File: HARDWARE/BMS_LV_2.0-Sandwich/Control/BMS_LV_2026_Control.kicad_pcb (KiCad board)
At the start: 4 copper layers, 62.5 x 36.4 mm, 59 parts, among them IC1 TAR5S33UTE85LF, IC2 M24M02E-UFMN6TP, IC4 TPS54202HDDCR, J1 Conn_01x26, U1 STM32G484RETx, U7 ADM3057ExRW, Y1 ATX-11-F-32.000MHZ-F05-T

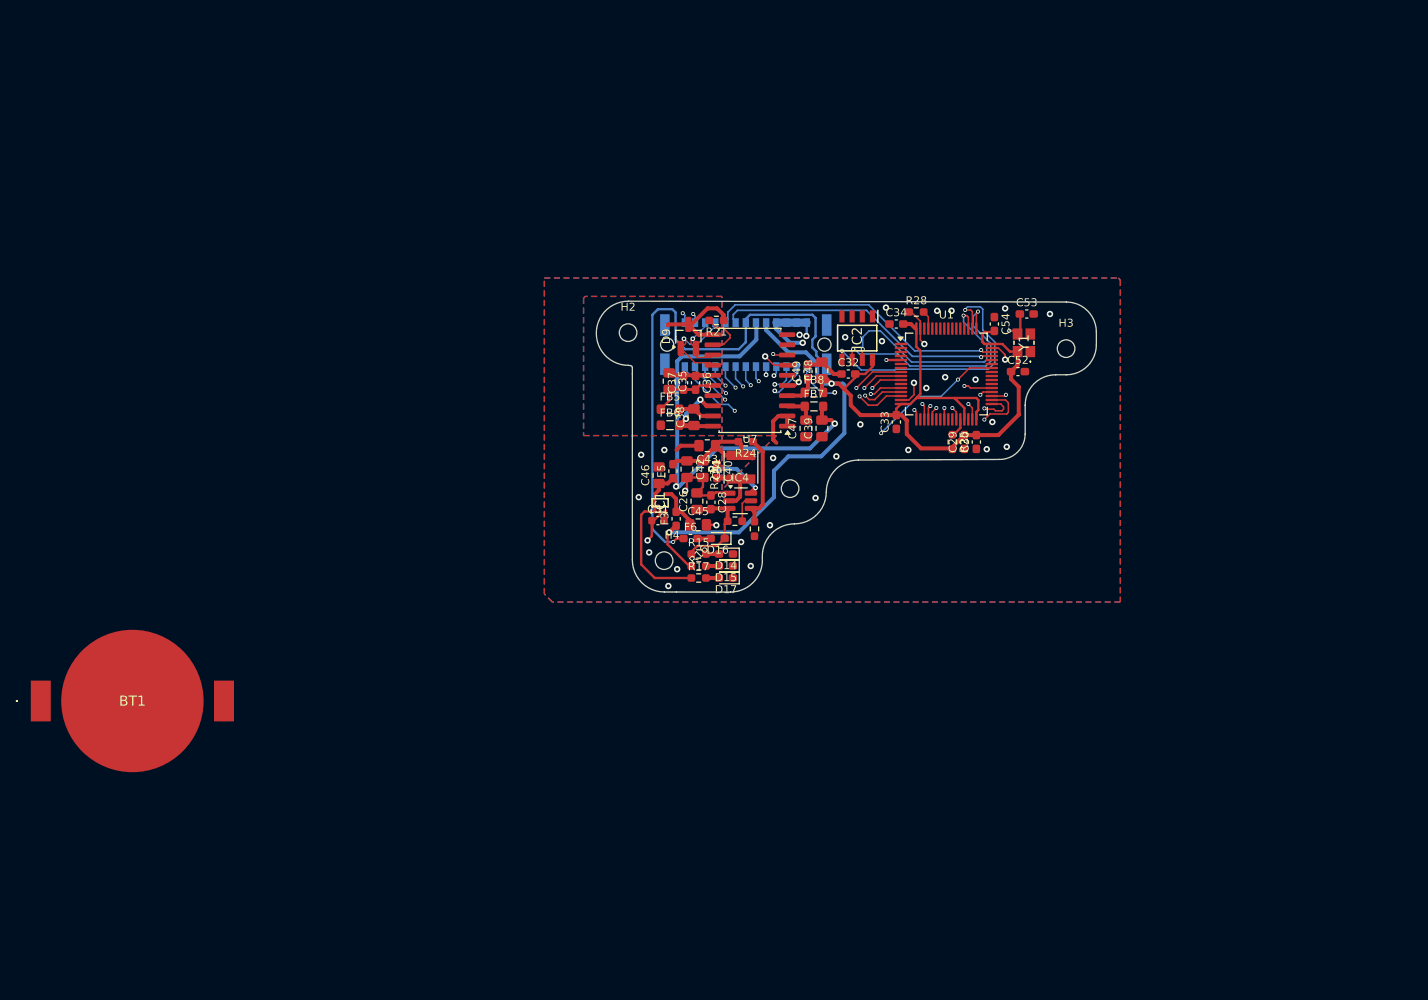
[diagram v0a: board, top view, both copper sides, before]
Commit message: Zmiany w power: nowe bezpieczniki, nowy wymienialny layout dla tych bezpiecznikow, dodano diode zenera dla stabilizacji napięcia, zmiany dla control:  wyjebany eeprom, przesunięty can, zmieniony layout przetwornic, dodano programator i tvs, jeszcze do dokonczenia routing w control.
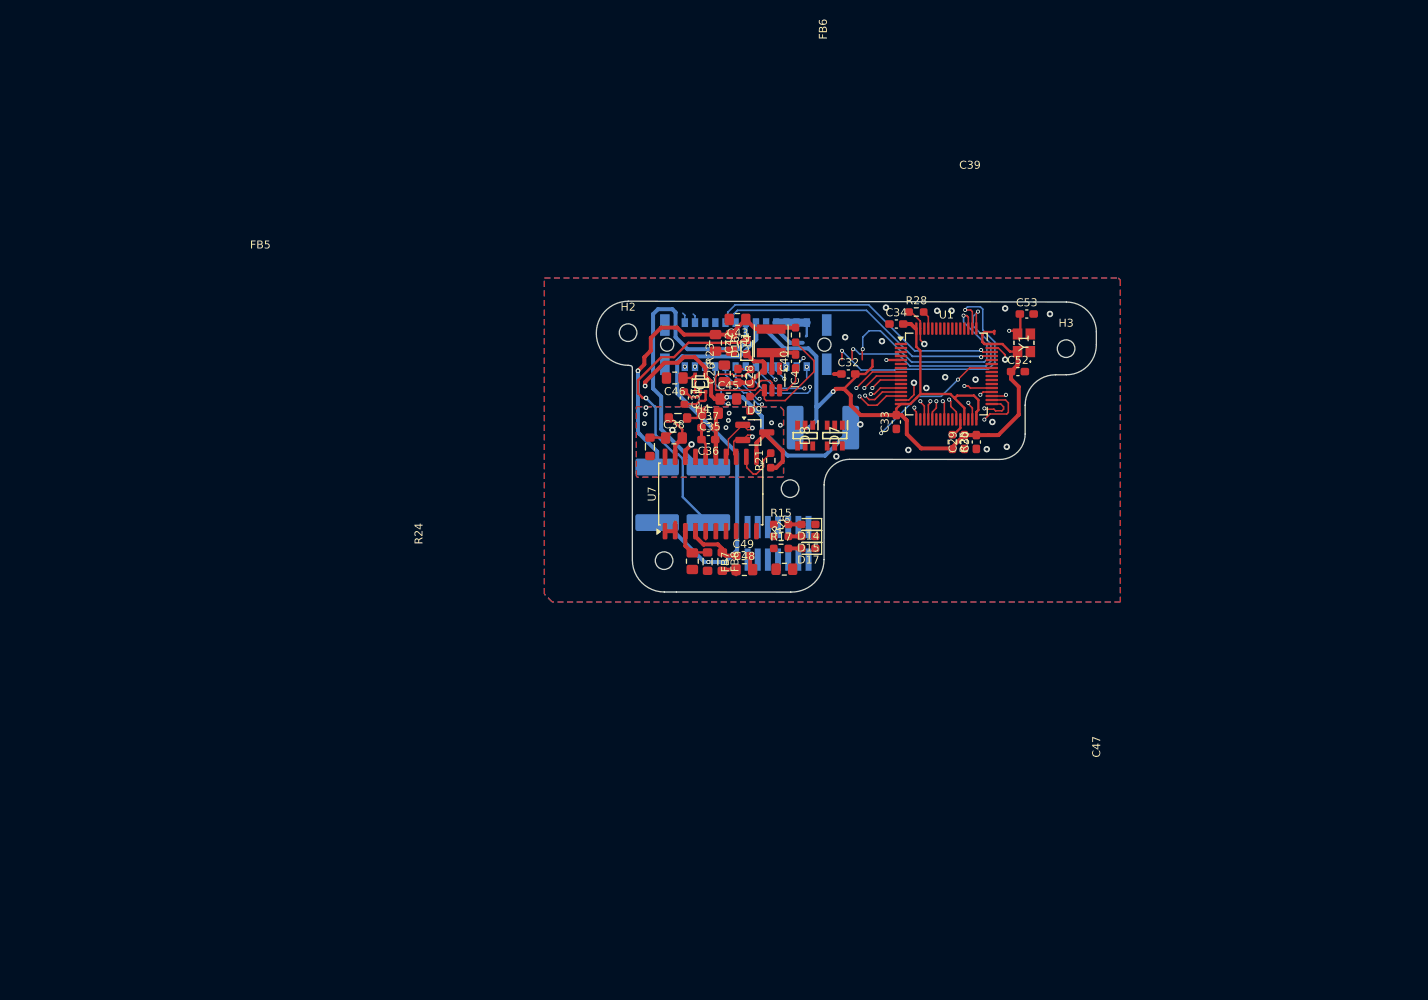
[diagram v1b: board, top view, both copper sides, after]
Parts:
- removed BT1: Battery_Cell, Footprint:BATHLD001
- removed C54: 100n, Capacitor_SMD:C_0603_1608Metric_Pad1.08x0.95mm_HandSolder
- removed F6: SF-0603FP050M-2, Fuse:Fuse_0603_1608Metric_Pad1.05x0.95mm_HandSolder
- removed IC2: M24M02E-UFMN6TP, Footprint:SOIC127P600X175-8N
- added D7: Quad TVS, Footprint:SOT95P285X140-6N, F.Cu at (167.3, 96.7)
- added D8: Quad TVS, Footprint:SOT95P285X140-6N, F.Cu at (163.6, 96.7)
- added F4: SMDH2920B150TF, Fuse:Fuse_2920_7451Metric_Pad2.10x5.45mm_HandSolder, B.Cu at (145.1, 104.1)
- added J3: FTSH-107-01-L-D-K, Footprint:FTSH-107-XX-YYY-DV-K, B.Cu at (160.2, 110.2)
- F3: value F0603G0R05FNTR -> SMDH2920B150TF; footprint Fuse:Fuse_0603_1608Metric_Pad1.05x0.95mm_HandSolder -> Fuse:Fuse_2920_7451Metric_Pad2.10x5.45mm_HandSolder; moved to B.Cu
- F5: value SF-0603FP050M-2 -> SMDH2920B150TF; footprint Fuse:Fuse_0603_1608Metric_Pad1.05x0.95mm_HandSolder -> Fuse:Fuse_2920_7451Metric_Pad2.10x5.45mm_HandSolder; moved to B.Cu
- R21: value 100K -> 0R
- R25, R28: value 1k -> 100k
- moved C48 26.7 mm to (156.0, 113.5), turned to 0 degrees
- moved C49 24.4 mm to (155.9, 111.7), turned to 0 degrees
- moved D16 24.2 mm to (156.3, 85.6), turned to 90 degrees
- moved FB8 24.1 mm to (153.2, 112.5), turned to -90 degrees
- moved FB7 23.5 mm to (151.4, 112.5), turned to -90 degrees
- moved C47 21.8 mm to (149.5, 112.4)
- moved F3 21.6 mm to (165.8, 95.7), turned to 0 degrees
- moved R21 18.8 mm to (159.3, 99.8), turned to 90 degrees
- moved C39 18.2 mm to (161.0, 113.4), turned to 180 degrees
- moved R22 18.2 mm to (156.8, 89.3), turned to -90 degrees
- moved C40 16.9 mm to (162.4, 87.4), turned to 90 degrees
- moved C26 16.3 mm to (153.5, 88.9)
- moved C43 16.2 mm to (155.1, 82.2)
- moved L4 16.2 mm to (159.4, 84.9)
- moved C41 16.2 mm to (154.4, 85.1)
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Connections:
- F5 pad 1: /5V -> VCC
- F5 pad 2: /Power/+5V_OUT -> Net-(D16-A)
- U1 pad 38: unconnected-(U1-PC6-Pad38) -> /Interlock
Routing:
- net Net-(D16-A): track 1.65 -> 37.6 mm, vias 0 -> 1
- net /3V3: track 141.1 -> 106.1 mm, vias 2 -> 1
- net /Power/VO_+3.3V: track 5.92 -> 37.4 mm, vias 0 -> 2
- net /Power/+5V_OUT: track 15.3 -> 42.0 mm, vias 0 -> 1
- net VCC: track 65.4 -> 43.0 mm, vias 1 -> 0
- net /5V: track 77.5 -> 56.4 mm, vias 2 -> 1
- net GND: track 55.3 -> 36.7 mm, vias 38 -> 21
- net /CAN/CAN_TX: track 39.8 -> 25.6 mm, vias 2 -> 1
- net /CAN/STBY_CAN_1: track 28.6 -> 15.7 mm, vias 2 -> 1
- net /SPI.MOSI: track 40.5 -> 27.8 mm
- net /SPI.MISO: track 38.3 -> 26.3 mm
- net /Power/EN: track 3.44 -> 15.4 mm
- net /SPI.SCK: track 35.6 -> 24.5 mm
- net Net-(C38-Pad1): track 12.3 -> 5.25 mm
- net /Therm_7: track 29.0 -> 23.2 mm
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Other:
- outline, holes or cut-outs redrawn

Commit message: Routing 65%
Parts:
- moved F4 11.8 mm to (154.7, 97.3), turned to 180 degrees
- moved F5 9.78 mm to (146.8, 95.5)
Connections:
- D7 pad 4: /Control/SWDIO -> /Control/SWCLK
- D7 pad 6: /Control/SWCLK -> /Control/SWDIO
- D8 pad 3: +3V3 -> /3V3
- D8 pad 4: /Control/URAT_TX -> /Control/URAT_RX
- D8 pad 6: /Control/URAT_RX -> /Control/URAT_TX
- R28 pad 2: Net-(U1-PB8) -> /Control/NRST
- U1 pad 10: /Therm_3 -> /Therm_8
- U1 pad 12: /Therm_4 -> /Therm_1
- U1 pad 13: /Therm_5 -> /Therm_2
- U1 pad 14: /Therm_6 -> /Therm_3
- U1 pad 17: /Therm_7 -> /Therm_4
- U1 pad 36: /Therm_8 -> /Therm_5
- U1 pad 49: /Control/I2C_SCL -> /Control/SWDIO
- U1 pad 50: /Control/I2C_SDA -> /Control/SWCLK
- U1 pad 51: /Control/I2C_WC -> unconnected-(U1-PA15-Pad51)
- U1 pad 52: unconnected-(U1-PC10-Pad52) -> /Control/URAT_RX
- U1 pad 53: unconnected-(U1-PC11-Pad53) -> /Control/URAT_TX
- U1 pad 61: Net-(U1-PB8) -> /Control/NRST
- U1 pad 8: /Therm_1 -> /Therm_8
- U1 pad 9: /Therm_2 -> /Therm_7
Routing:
- net /Control/URAT_RX: track 0.00 -> 54.3 mm, vias 0 -> 3
- net /Switch_Signal: track 50.3 -> 0.00 mm, vias 1 -> 0
- net /Control/URAT_TX: track 0.00 -> 46.8 mm, vias 0 -> 3
- net /Control/NRST: track 0.00 -> 43.9 mm, vias 0 -> 4
- net /VoltageFuseMeasure: track 43.0 -> 0.00 mm, vias 1 -> 0
- net /Control/SWCLK: track 0.00 -> 43.0 mm, vias 0 -> 3
- net /Control/SWDIO: track 0.00 -> 40.0 mm, vias 0 -> 3
- net /Therm_1: track 40.0 -> 0.00 mm, vias 2 -> 0
- net /Control/I2C_SDA: track 34.6 -> 0.00 mm, vias 2 -> 0
- net /Therm_3: track 34.4 -> 0.00 mm, vias 2 -> 0
- net /Therm_2: track 34.1 -> 0.00 mm, vias 2 -> 0
- net /Therm_8: track 32.0 -> 0.00 mm, vias 2 -> 0
- net /Therm_4: track 29.6 -> 0.00 mm, vias 2 -> 0
- net /Control/I2C_SCL: track 29.3 -> 0.00 mm, vias 2 -> 0
- net /Control/I2C_WC: track 29.2 -> 0.00 mm, vias 2 -> 0
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
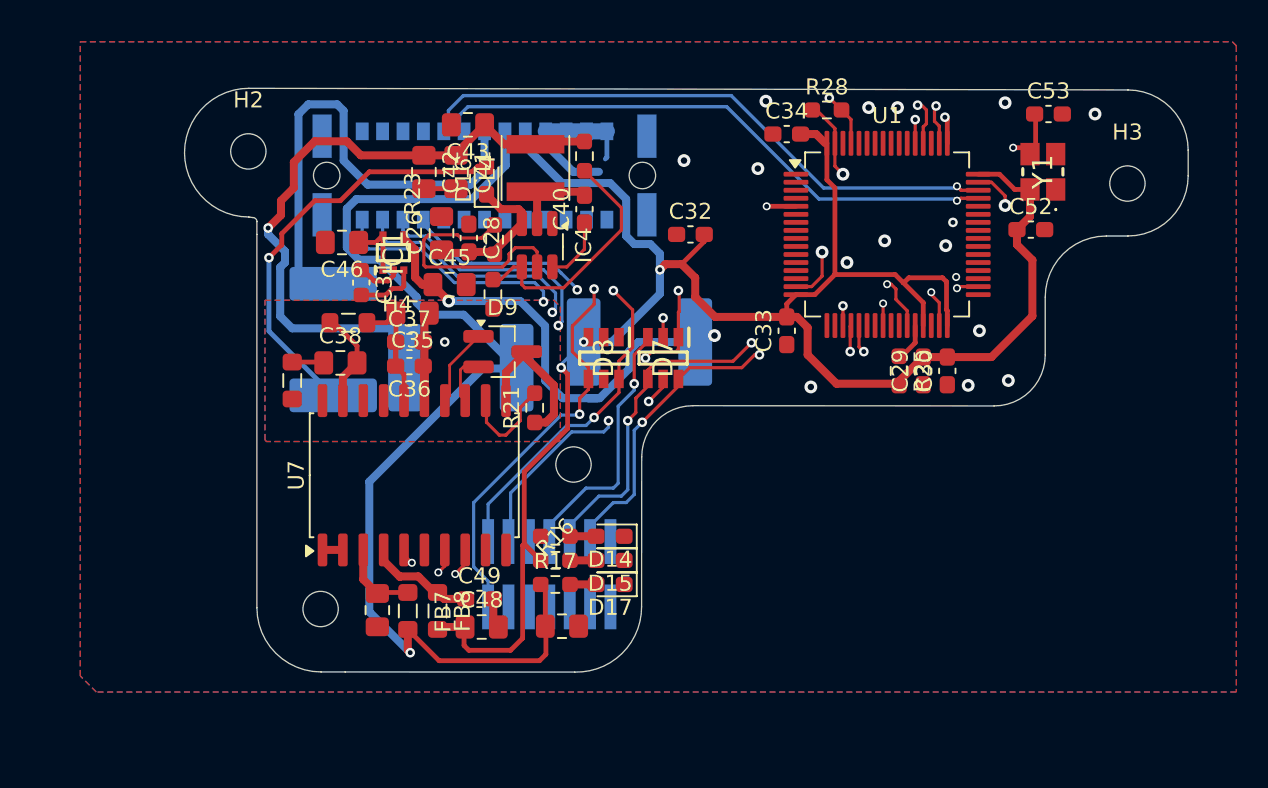
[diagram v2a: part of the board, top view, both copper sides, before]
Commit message: Pierwsza wersja bez błędów DRC/ERC, skończony routing plytki control
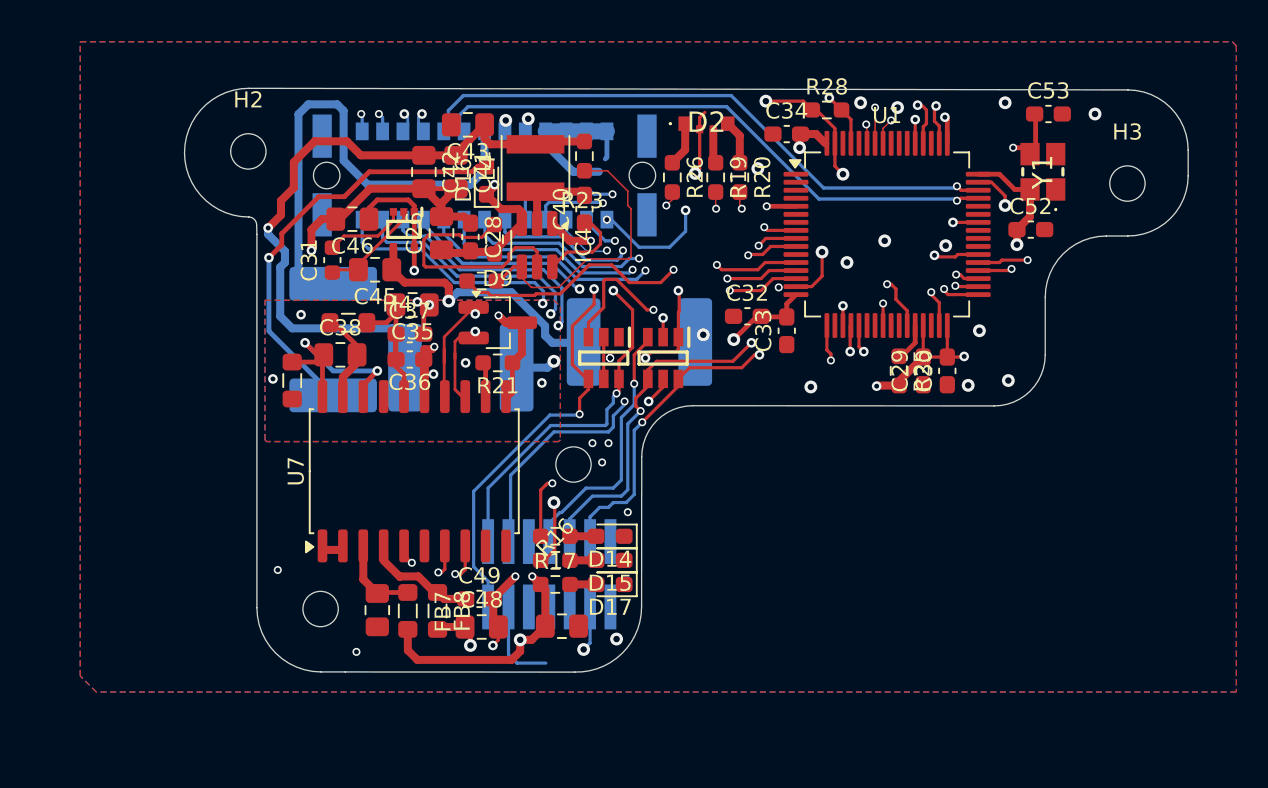
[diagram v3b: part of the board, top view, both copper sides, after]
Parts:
- added D2: LED_BKGR, Footprint:APFA2507LSURKSYKZGKC, F.Cu at (170.0, 82.1)
- added R19: 750R, Resistor_SMD:R_0603_1608Metric_Pad0.98x0.95mm_HandSolder, F.Cu at (170.6, 85.5)
- added R20: 750R, Resistor_SMD:R_0603_1608Metric_Pad0.98x0.95mm_HandSolder, F.Cu at (172.1, 85.5)
- added R26: 750R, Resistor_SMD:R_0603_1608Metric_Pad0.98x0.95mm_HandSolder, F.Cu at (167.9, 85.5)
- moved C32 6.21 mm to (172.6, 94.1)
- moved C45 4.73 mm to (149.4, 91.2), turned to 180 degrees
- moved R21 3.62 mm to (157.0, 97.0), turned to 180 degrees
- moved C31 2.28 mm to (146.7, 90.6), turned to 90 degrees
- moved D9 1.82 mm to (157.0, 94.5)
- moved IC1 1.59 mm to (151.2, 88.7), turned to -90 degrees
- moved C46 1.59 mm to (147.9, 88.0)
- moved R23 1.08 mm to (156.0, 91.9), turned to 0 degrees
- moved C35 0.51 mm to (151.7, 93.4)
- moved C38 0.50 mm to (147.2, 96.5)
- moved C37 0.49 mm to (151.5, 95.2)
- moved C36 0.41 mm to (151.5, 96.8)
- moved U7 0.25 mm to (151.8, 103.8)
- moved C28 0.12 mm to (155.3, 89.2)
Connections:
- F3 pad 1: /3V3 -> /Power/VO_+3.3V
- F3 pad 2: /Power/VO_+3.3V -> /3V3
- J3 pad 3: +3V3 -> /3V3
- U1 pad 1: /Control/VBat -> unconnected-(U1-VBAT-Pad1)
- U1 pad 57: unconnected-(U1-PB4-Pad57) -> /Control/RED
- U1 pad 58: unconnected-(U1-PB5-Pad58) -> /Control/GREEN
- U1 pad 59: unconnected-(U1-PB6-Pad59) -> /Control/YELLOW
- U1 pad 8: /Therm_8 -> /Therm_6
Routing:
- net /3V3: track 123.6 -> 44.3 mm, vias 3 -> 11
- net GND: track 36.9 -> 92.0 mm, vias 22 -> 36
- net /VoltageFuseMeasure: track 0.00 -> 48.5 mm, vias 0 -> 2
- net /Switch_Signal: track 0.00 -> 44.8 mm, vias 0 -> 2
- net /Therm_5: track 0.00 -> 36.6 mm, vias 0 -> 2
- net /5V: track 72.2 -> 40.5 mm, vias 1 -> 5
- net /Therm_4: track 0.00 -> 28.6 mm, vias 0 -> 2
- net /Interlock: track 0.00 -> 27.0 mm, vias 0 -> 3
- net /Power/+24V safe: track 8.99 -> 35.3 mm, vias 0 -> 2
- net /Therm_3: track 0.00 -> 25.4 mm, vias 0 -> 2
- net /Therm_1: track 0.00 -> 25.0 mm, vias 0 -> 2
- net /CAN-: track 3.24 -> 26.9 mm, vias 0 -> 2
- net /Therm_2: track 0.00 -> 23.7 mm, vias 0 -> 2
- net /CAN+: track 4.87 -> 26.9 mm, vias 0 -> 2
- net /Control/RED: track 0.00 -> 19.2 mm, vias 0 -> 2
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- added copper zone on In3.Cu, net /3V3
- added copper zone on In3.Cu, net /5V
- added copper zone on In3.Cu, net /CAN/gnd_iso
- added copper zone on In4.Cu, net /CAN/gnd_iso
- added copper zone on In3.Cu, net GND
- added copper zone on In4.Cu, net GND
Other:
- outline, holes or cut-outs redrawn
- copper layers 4 -> 6

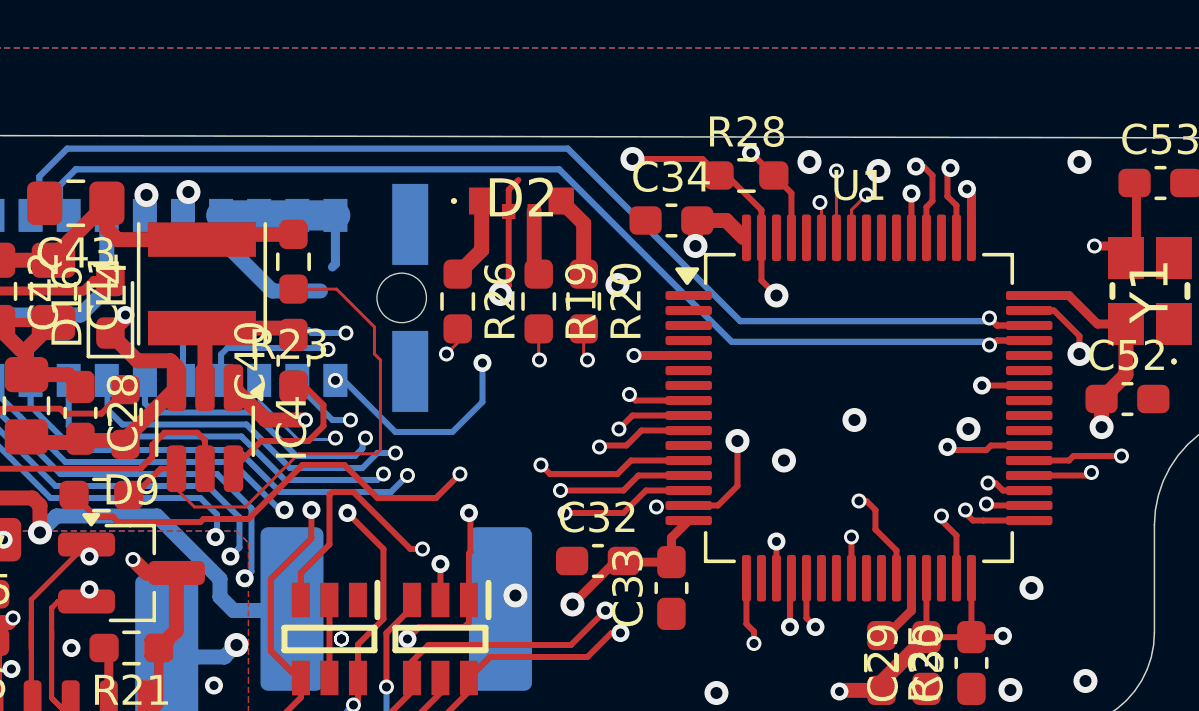
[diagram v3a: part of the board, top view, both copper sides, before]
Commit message: Przesunięcie sciezek z jednej warstwy wew aby zwolnic ja na mase
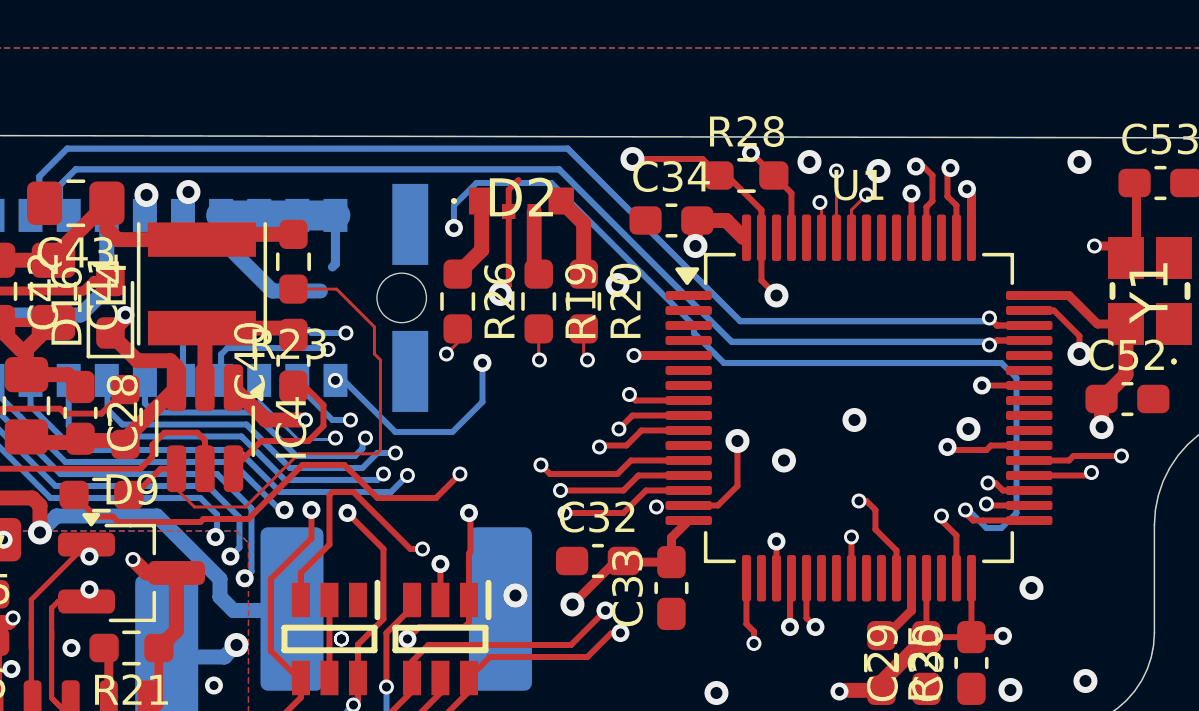
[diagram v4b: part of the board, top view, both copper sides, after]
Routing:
- net /Switch_Signal: track 44.8 -> 54.9 mm, vias 2 -> 3
- net /5V: track 40.5 -> 49.0 mm
- net /VoltageFuseMeasure: track 48.5 -> 50.4 mm
